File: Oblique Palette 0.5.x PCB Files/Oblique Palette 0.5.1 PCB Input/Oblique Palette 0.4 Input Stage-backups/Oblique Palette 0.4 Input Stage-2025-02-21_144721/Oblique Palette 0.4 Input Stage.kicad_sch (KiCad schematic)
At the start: 18 parts, among them J16 Conn_01x03_Female_Pin, J17 AudioJack2_SwitchT, U3 MCP6004

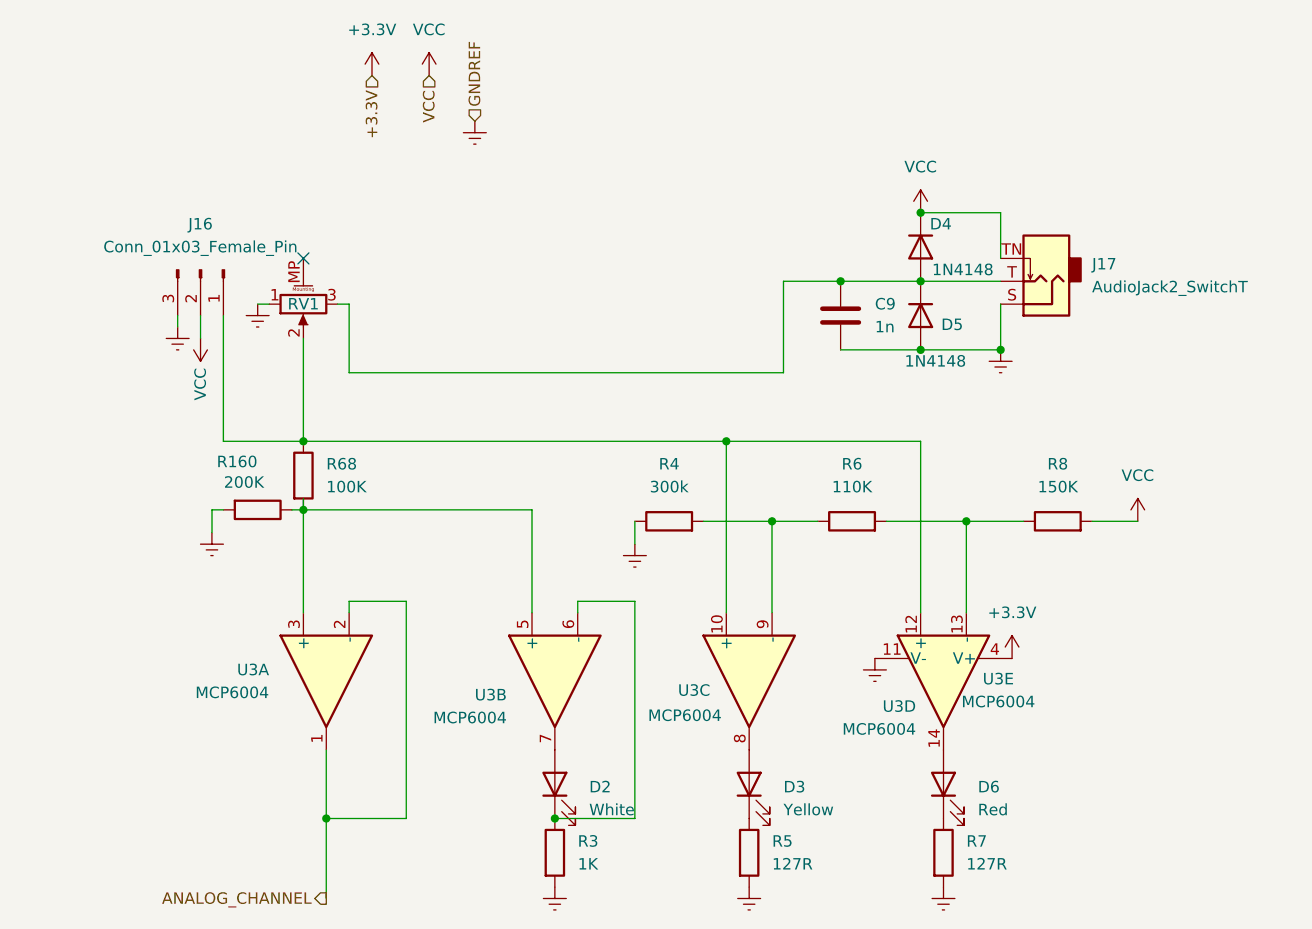
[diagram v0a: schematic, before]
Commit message: Associated Input and Output tiles relatively rather than absolutely, which got them lost in the sauce.
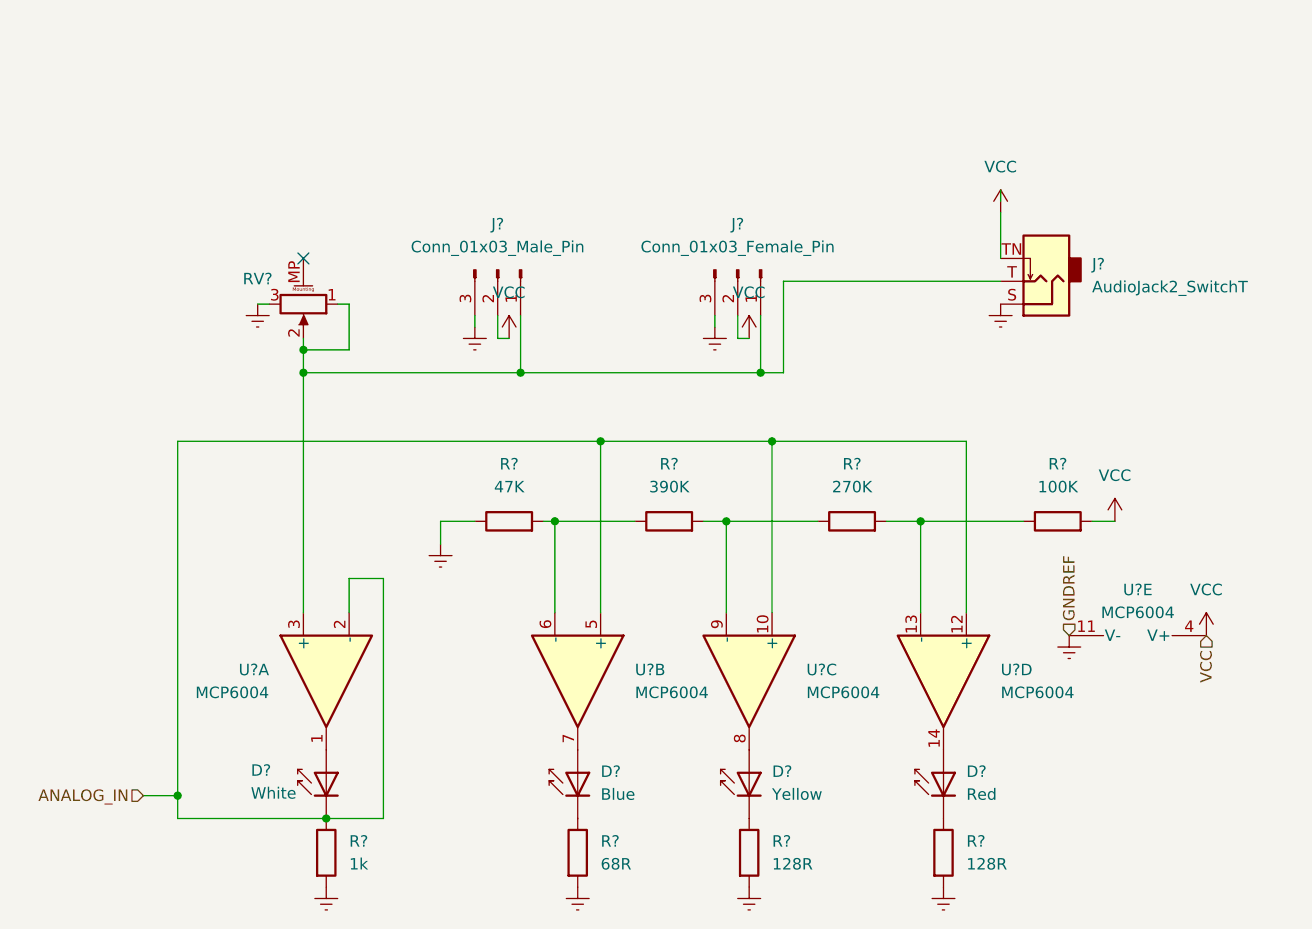
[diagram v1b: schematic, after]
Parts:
- removed C9: 1n, Capacitor_SMD:C_0805_2012Metric, symbol Device:C
- removed D4, D5: 1N4148, Diode_SMD:D_SOD-123, symbol Device:D
- removed R160: 200K, Resistor_SMD:R_0805_2012Metric, symbol Device:R
- removed R68: 100K, Resistor_SMD:R_0805_2012Metric, symbol Device:R
- added D?: White, LED_THT:LED_SideEmitter_Rectangular_W4.5mm_H1.6mm, symbol LED:IRL81A
- added J?: Conn_01x03_Male_Pin, Connector_PinHeader_2.54mm:PinHeader_1x03_P2.54mm_Vertical, symbol Connector:Conn_01x03_Pin
- added R?: 47K, Resistor_THT:R_Axial_DIN0207_L6.3mm_D2.5mm_P2.54mm_Vertical, symbol Device:R
- added R?: 1k, Resistor_THT:R_Axial_DIN0207_L6.3mm_D2.5mm_P2.54mm_Vertical, symbol Device:R
- D?: renamed from D2; value White -> Blue; footprint LED_THT:LED_Rectangular_W5.0mm_H2.0mm -> LED_THT:LED_SideEmitter_Rectangular_W4.5mm_H1.6mm; symbol Device:LED -> LED:IRL81A
- D?: renamed from D3; footprint LED_THT:LED_Rectangular_W5.0mm_H2.0mm -> LED_THT:LED_SideEmitter_Rectangular_W4.5mm_H1.6mm; symbol Device:LED -> LED:IRL81A
- D?: renamed from D6; footprint LED_THT:LED_Rectangular_W5.0mm_H2.0mm -> LED_THT:LED_SideEmitter_Rectangular_W4.5mm_H1.6mm; symbol Device:LED -> LED:IRL81A
- R?: renamed from R7; value 127R -> 128R; footprint Resistor_SMD:R_0805_2012Metric -> Resistor_THT:R_Axial_DIN0207_L6.3mm_D2.5mm_P2.54mm_Vertical
- R?: renamed from R3; value 1K -> 68R; footprint Resistor_SMD:R_0805_2012Metric -> Resistor_THT:R_Axial_DIN0207_L6.3mm_D2.5mm_P2.54mm_Vertical
- R?: renamed from R5; value 127R -> 128R; footprint Resistor_SMD:R_0805_2012Metric -> Resistor_THT:R_Axial_DIN0207_L6.3mm_D2.5mm_P2.54mm_Vertical
- R?: renamed from R6; value 110K -> 270K; footprint Resistor_SMD:R_0805_2012Metric -> Resistor_THT:R_Axial_DIN0207_L6.3mm_D2.5mm_P2.54mm_Vertical
- R?: renamed from R8; value 150K -> 100K; footprint Resistor_SMD:R_0805_2012Metric -> Resistor_THT:R_Axial_DIN0207_L6.3mm_D2.5mm_P2.54mm_Vertical
- R?: renamed from R4; value 300k -> 390K; footprint Resistor_SMD:R_0805_2012Metric -> Resistor_THT:R_Axial_DIN0207_L6.3mm_D2.5mm_P2.54mm_Vertical
- U? (x5): renamed from U3; footprint Package_SO:SOIC-14_3.9x8.7mm_P1.27mm -> Package_DIP:DIP-14_W7.62mm_Socket_LongPads; LCSC PN C116668 -> (none)
- renumbered J16 to J?, J17 to J?, RV1 to RV?
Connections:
- net +3.3V is gone; now on net VCC: U?.4 (V+)
- net GNDREF: now also RV?.3, J?.3 (Pin_3), R?.1, R?.2; no longer R?.1, RV?.1
- net VCC: now also J?.2 (Pin_2)
- net at J?.1 (Pin_1), RV?.2: now also J?.T, RV?.1, U?.3 (+), J?.1 (Pin_1); no longer U?.10 (+), U?.12 (+)
- net ANALOG_IN: now reaches U?.5 (+)
- net ANALOG_IN: now also U?.10 (+), U?.12 (+), U?.2 (-), D?.1 (K), R?.1; no longer U?.3 (+)
- net at D?.1 (K), R?.1: no longer U?.6 (-)
- net ANALOG_CHANNEL: no longer names the net of U?.1
- net ANALOG_CHANNEL: now also D?.2 (A); no longer U?.2 (-)
- new net: R?.1, R?.2, U?.6 (-)
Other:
- moved on the sheet: J?, R?, RV?, U?B, U?C, U?D, U?E
